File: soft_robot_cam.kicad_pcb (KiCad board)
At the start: 4 copper layers, 49.8 x 47.3 mm, 95 parts, among them J1 Connector, J10 Screw_Terminal_01x02, J11 Conn_02x02_Counter_Clockwise, J2 Conn_01x06, J3 Conn_01x03, J4 Conn_01x05_Pin, J5 Conn_01x02_Pin, J6 Screw_Terminal_01x02, J7 Screw_Terminal_01x02, J8 Conn_01x24_Socket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

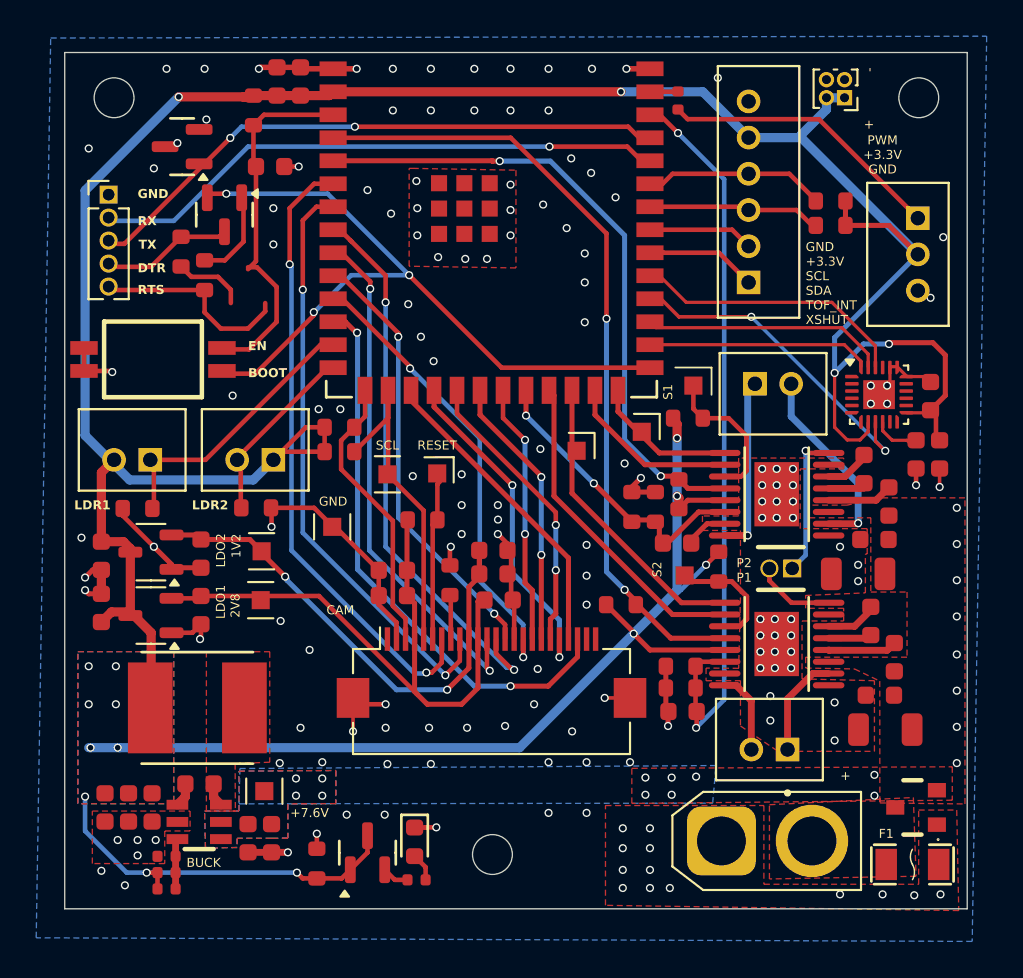
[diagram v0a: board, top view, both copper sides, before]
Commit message: Minor additions to PCB Layout, added branding and text
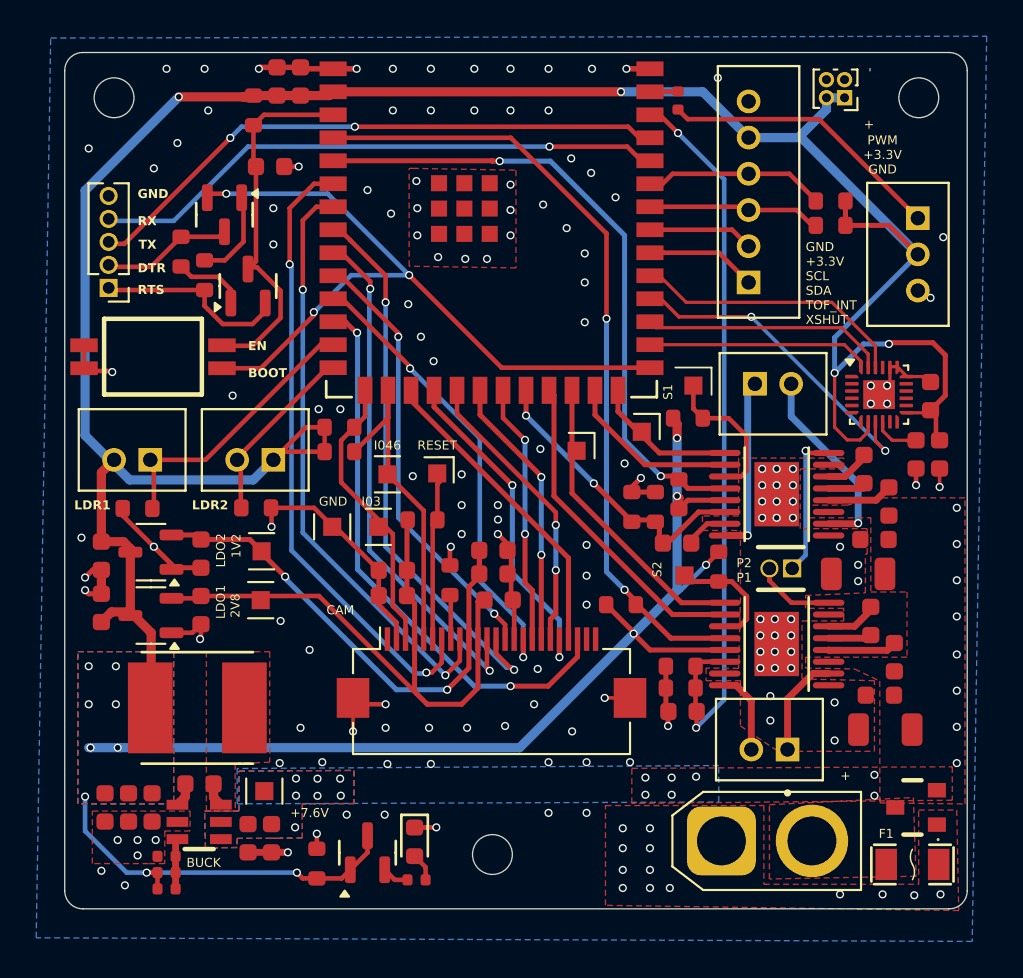
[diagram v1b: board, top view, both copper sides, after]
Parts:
- added G***: LOGO, LOGO, B.Cu at (164.4, 130.0)
- added GND: TestPoint_Pad_1.0x1.0mm, TestPoint:TestPoint_Pad_1.0x1.0mm, F.Cu at (175.6, 141.4)
- moved Q1 8.52 mm to (168.4, 128.1), turned to 90 degrees
- moved J4 5.15 mm to (160.7, 128.2), turned to 180 degrees
- moved SW4 0.15 mm to (163.2, 132.0)
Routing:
- net +7.6V: vias 11 -> 14
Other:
- outline, holes or cut-outs redrawn
- board text added: "Designed by: Evan Bhogal https://github.com/esb8/Soft-Robotics"
- board text added: "I03"
- board text added: "I046"
- board text added: "PROPERTY OF ELIXIR LABS"
- board text removed: "SCL"

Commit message: Minor Changes
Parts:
- removed the GND at (173.1, 141.4)
- removed the GND at (175.6, 141.4)
- removed the GND at (176.1, 138.5)
- added R25: 10kΩ, PCM_JLCPCB:R_0603, F.Cu at (191.8, 135.6)
- added REF**: TestPoint_Pad_1.0x1.0mm, TestPoint:TestPoint_Pad_1.0x1.0mm, F.Cu at (173.1, 141.4)
- added REF**: TestPoint_Pad_1.0x1.0mm, TestPoint:TestPoint_Pad_1.0x1.0mm, F.Cu at (176.1, 138.4)
- added REF**: TestPoint_Pad_1.0x1.0mm, TestPoint:TestPoint_Pad_1.0x1.0mm, F.Cu at (175.6, 141.4)
- moved G*** 3.13 mm to (165.4, 132.9)
- moved REF** 0.66 mm to (192.9, 132.9)
- moved R16 0.52 mm to (193.2, 135.6), turned to 90 degrees
- moved GND 0.35 mm to (186.5, 137.6)
- moved R9 0.15 mm to (162.2, 140.4)
- moved GND 0.11 mm to (190.1, 136.2)
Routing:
- net /IN1_A: track 8.02 -> 9.79 mm
- net GND: track 65.5 -> 66.5 mm
- net +3.3V: track 222.8 -> 223.4 mm
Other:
- board text added: "IN1B"
- board text added: "IO3"
- board text added: "IO45"
- board text added: "IO46"
- board text added: "PWM"
- board text added: "REDESIGN"
- board text added: "SCL"
- board text added: "SDA"
- board text added: "TOF_INT"
- board text added: "XSHUT"
- board text removed: "I03"
- board text removed: "I046"

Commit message: Cleaned Up BOM
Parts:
- F1: value JFC1206-1450FS -> BHFUSE BSMD1206C-1700T
- J8: footprint Connector_FFC-FPC:Hirose_FH12-24S-0.5SH_1x24-1MP_P0.50mm_Horizontal -> easyeda2kicad:FPC-SMD_AFC07-S24ECA-00
- L1: footprint easyeda2kicad:IND-SMD_L6.0-W6.0_SWPA6045S -> easyeda2kicad:IND-SMD_L6.0-W6.0
- moved J8 0.78 mm to (181.9, 148.7)
- moved F1 0.35 mm to (205.1, 159.7)
- moved L1 0.32 mm to (165.3, 151.5)
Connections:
- U9 pad 42: GND -> (no net)
- U9 pad 43: GND -> (no net)
- U9 pad 44: GND -> (no net)
- U9 pad 45: GND -> (no net)
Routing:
- net GND: track 66.5 -> 71.1 mm, vias 164 -> 160
- net +2V8: track 34.6 -> 35.4 mm, vias 0 -> 2
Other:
- board text removed: "REDESIGN"

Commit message: Critical Fixes
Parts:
- removed the REF** at (176.1, 138.4)
- added G***: LOGO, LOGO, B.Cu at (181.2, 121.2)
- moved R25 2.65 mm to (189.2, 135.6), turned to 0 degrees
- moved R3 1.70 mm to (173.4, 137.6)
- moved GND 1.52 mm to (191.5, 135.8)
- moved R24 1.45 mm to (173.4, 135.8)
- moved REF** 0.75 mm to (178.8, 139.2)
- moved C25 0.36 mm to (182.2, 145.1)
- moved F1 0.33 mm to (205.1, 160.0)
- moved C26 0.24 mm to (181.9, 142.5)
- moved C31 0.20 mm to (182.0, 143.8)
- moved REF** 0.10 mm to (193.0, 132.9)
- moved R23 0.05 mm to (200.6, 124.8)
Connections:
- R24 pad 2: /I2C_SCL -> /I2C_SDA
- R25 pad 1: /IN1_A -> GND
- R25 pad 2: GND -> Net-(U9-IO45)
- R3 pad 2: /I2C_SDA -> /I2C_SCL
- U9 pad 14: /LDR2 -> /I2C_SDA
- U9 pad 15: /I2C_SDA -> /I2C_SCL
- U9 pad 16: /I2C_SCL -> /LDR2
- U9 pad 26: /IN1_A -> Net-(U9-IO45)
- U9 pad 28: /MOSI1 -> /IN1_A
- U9 pad 29: /SCLK1 -> /MOSI1
- U9 pad 30: /MISO1 -> /SCLK1
- U9 pad 31: /CS1 -> /MISO1
- U9 pad 32: /XSHUT -> /CS1
- U9 pad 33: /TOF_INT -> /XSHUT
- U9 pad 42: (no net) -> GND
- U9 pad 43: (no net) -> GND
- U9 pad 44: (no net) -> GND
- U9 pad 45: (no net) -> GND
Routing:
- net /LDR2: track 10.2 -> 18.5 mm, vias 0 -> 2
- net /TOF_INT: track 5.98 -> 0.00 mm
- net +3.3V: track 223.4 -> 220.5 mm
- net /I2C_SCL: track 18.7 -> 16.3 mm
- net Net-(U9-IO45): track 0.00 -> 2.23 mm
- net /I2C_SDA: track 15.8 -> 17.5 mm
- net GND: track 71.1 -> 72.3 mm, vias 160 -> 161
- net /MOSI1: track 12.3 -> 13.3 mm
- net /CS1: track 15.2 -> 15.8 mm
- net /MISO1: track 18.3 -> 18.8 mm
- net /SCLK1: track 13.5 -> 14.0 mm
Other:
- board text removed: "IO45"
- board text removed: "IO46"
- board text removed: "PROPERTY OF ELIXIR LABS"

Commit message: Fixes the layout
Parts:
- removed J2: Conn_01x06, easyeda2kicad:JST_B6B-PH-K-S
- added J12: B5B-PH-K-S-(LF)(SN), easyeda2kicad:CONN-TH_B5B-PH-K-S-LF-SN, F.Cu at (196.0, 121.8)
- added R26: 10kΩ, PCM_JLCPCB:R_0603, F.Cu at (176.3, 136.5)
- moved C13 3.86 mm to (166.6, 119.1), turned to 180 degrees
- moved REF** 2.50 mm to (176.3, 139.0)
- moved R18 0.96 mm to (192.2, 116.9), turned to 90 degrees
- moved R25 0.07 mm to (189.1, 135.6)
- turned GND to -90 degrees
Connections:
- REF** pad : /I2C_SDA -> /I2C_SCL
- U9 pad 16: /LDR2 -> Net-(U9-IO46)
- U9 pad 33: /XSHUT -> /nFAULT_A
- U9 pad 5: /nFAULT_A -> /LDR2
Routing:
- net /nFAULT_A: track 35.7 -> 19.3 mm
- net /XSHUT: track 6.81 -> 0.00 mm
- net /LDR2: track 18.5 -> 25.3 mm, vias 2 -> 1
- net +3.3V: track 220.5 -> 226.4 mm
- net Net-(U9-IO46): track 0.00 -> 2.01 mm
- net /EN: track 20.0 -> 21.4 mm
- net GND: track 72.3 -> 73.5 mm, vias 161 -> 160
- net /S_PWM: track 15.7 -> 16.4 mm
- net /BOOT: track 40.5 -> 41.2 mm
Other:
- board text removed: "TOF_INT"
- board text removed: "XSHUT"

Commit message: Production ready PCB
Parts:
- removed J11: Conn_02x02_Counter_Clockwise, Connector_PinHeader_1.00mm:PinHeader_2x02_P1.00mm_Vertical
- added REF**: TestPoint_Pad_1.0x1.0mm, TestPoint:TestPoint_Pad_1.0x1.0mm, F.Cu at (178.2, 137.0)
- added U1: PZ127-2-02-Z, easyeda2kicad:HDR-TH_4P-P1.27-V-M-R2-C2-S1.27_MH127V-12-04-0820, F.Cu at (200.9, 117.4)
- moved REF** 0.22 mm to (176.4, 139.2)
- moved G*** 0.07 mm to (165.4, 133.0)
- turned REF** to -90 degrees
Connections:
- J12 pad 1: +3.3V -> /XSHUT
- U3 pad 22: /CS1 -> +3.3V
- U3 pad 23: /SCLK1 -> /SCL
- U3 pad 24: /MOSI1 -> /SDA
- U3 pad 9: /MISO1 -> unconnected-(U3-SDO/AD0-Pad9)
- U9 pad 28: /IN1_A -> unconnected-(U9-IO35-Pad28)
- U9 pad 29: /MOSI1 -> unconnected-(U9-IO36-Pad29)
- U9 pad 30: /SCLK1 -> unconnected-(U9-IO37-Pad30)
- U9 pad 31: /MISO1 -> /IN1_A
- U9 pad 32: /CS1 -> /nFAULT_A
- U9 pad 33: /nFAULT_A -> /XSHUT
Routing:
- net /MISO1: track 18.8 -> 0.00 mm, vias 2 -> 0
- net /CS1: track 15.8 -> 0.00 mm
- net /SCLK1: track 14.0 -> 0.00 mm
- net /MOSI1: track 13.3 -> 0.00 mm
- net /SCL: track 10.2 -> 20.6 mm
- net /SDA: track 9.59 -> 18.4 mm
- net /XSHUT: track 0.00 -> 6.34 mm
- net +3.3V: track 226.4 -> 222.0 mm
- net /IN1_A: track 9.99 -> 13.7 mm
- net Net-(U9-IO46): track 2.01 -> 4.16 mm
- net /nFAULT_A: track 19.3 -> 17.8 mm
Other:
- board text added: "GND +3.3V SCL SDA +3.3V"
- board text added: "IO46"
- board text removed: "GND +3.3V SCL SDA TOF_INT XSHUT"

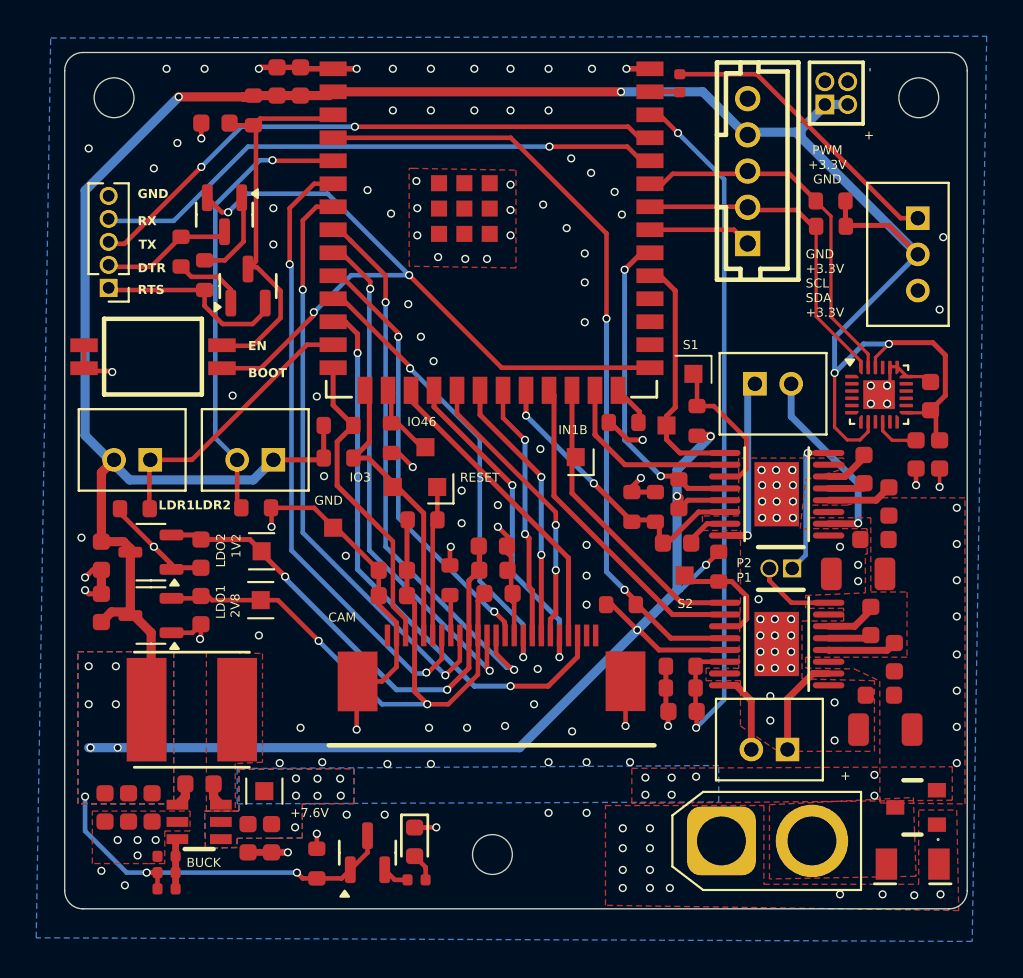
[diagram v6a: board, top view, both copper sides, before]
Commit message: Fixed Fuse, Added more testpads, changed xt30 to male, added switch in schematic for GPIO3
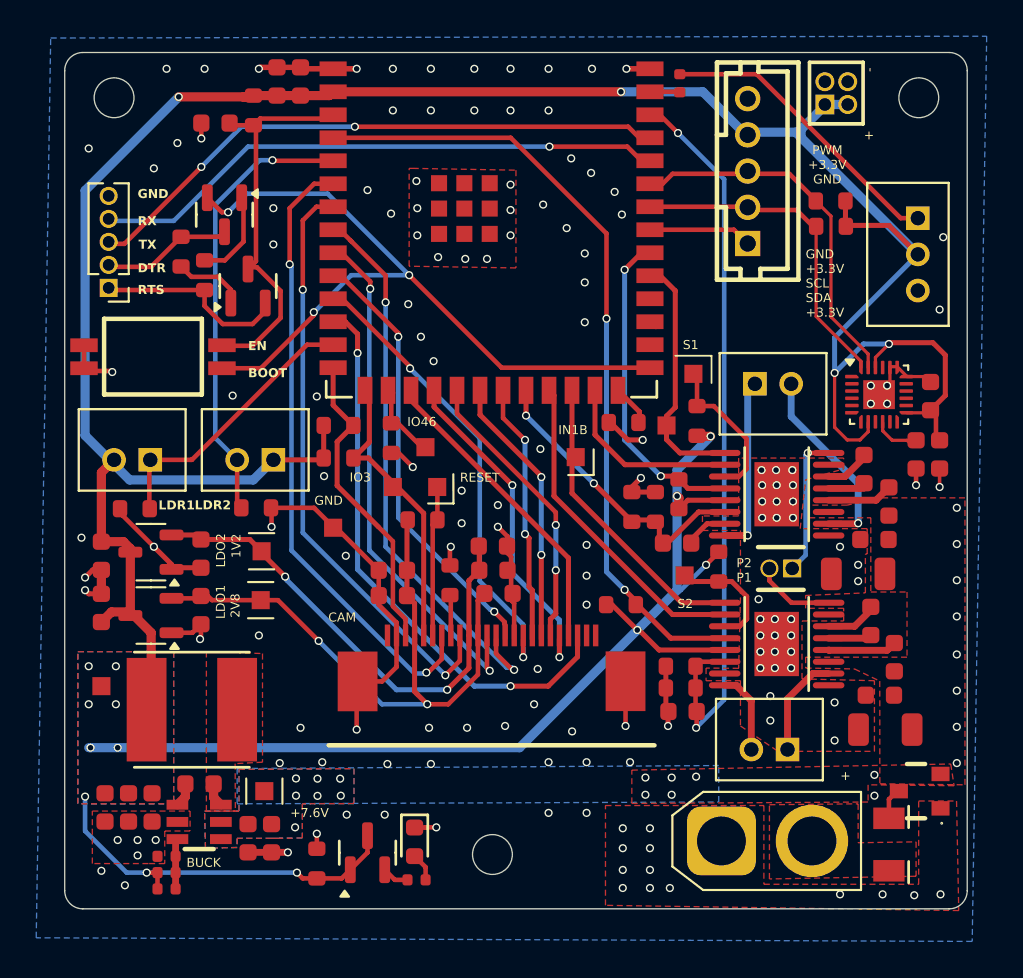
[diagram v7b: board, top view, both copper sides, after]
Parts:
- added REF**: TestPoint_Pad_1.0x1.0mm, TestPoint:TestPoint_Pad_1.0x1.0mm, F.Cu at (160.3, 150.2)
- moved F1 1.70 mm to (203.8, 158.9), turned to 90 degrees
- moved Q3 0.92 mm to (205.5, 156.0)
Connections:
- F1 pad 2: GND -> Net-(Q3-D)
- Q3 pad 3: Net-(J1-Pin_2) -> Net-(Q3-D)
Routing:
- net Net-(Q3-D): track 0.00 -> 1.66 mm
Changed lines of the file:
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@@
 	(net 87 "unconnected-(U9-IO37-Pad30)")
 	(net 88 "/XSHUT")
+	(net 89 "Net-(Q3-D)")
 	(footprint "PCM_JLCPCB:C_0603"
 		(layer "F.Cu")
@@
 		)
 	)
+	(footprint "TestPoint:TestPoint_Pad_1.0x1.0mm"
+		(layer "F.Cu")
+		(at 160.3 150.2)
+		(descr "SMD rectangular pad as test Point, square 1.0mm side length")
+		(tags "test point SMD pad rectangle square")
+		(property "Reference" "REF**"
+			(at 0 -1.448 0)
+			(layer "F.SilkS")
+			(hide yes)
+			(effects
+				(font
+					(size 1 1)
+					(thickness 0.153)
+				)
+			)
+		)
+		(property "Value" "TestPoint_Pad_1.0x1.0mm"
+			(at 0 1.55 0)
+			(layer "F.Fab")
+			(effects
+				(font
+					(size 1 1)
+					(thickness 0.153)
+				)
+			)
+		)
+		(property "Datasheet" ""
+			(at 0 0 0)
+			(unlocked yes)
+			(layer "F.Fab")
+			(hide yes)
+			(effects
+				(font
+					(size 1.27 1.27)
+					(thickness 0.153)
+				)
+			)
+		)
+		(property "Description" ""
+			(at 0 0 0)
+			(unlocked yes)
+			(layer "F.Fab")
+			(hide yes)
+			(effects
+				(font
+					(size 1.27 1.27)
+					(thickness 0.153)
+				)
+			)
+		)
+		(attr exclude_from_pos_files exclude_from_bom)
+		(fp_line
+			(start -1 -1)
+			(end -1 1)
+			(stroke
+				(width 0.05)
+				(type solid)
+			)
+			(layer "F.CrtYd")
+		)
+		(fp_line
+			(start -1 -1)
+			(end 1 -1)
+			(stroke
+				(width 0.05)
+				(type solid)
+			)
+			(layer "F.CrtYd")
+		)
+		(fp_line
+			(start 1 1)
+			(end -1 1)
+			(stroke
+				(width 0.05)
+				(type solid)
+			)
+			(layer "F.CrtYd")
+		)
+		(fp_line
+			(start 1 1)
+			(end 1 -1)
+			(stroke
+				(width 0.05)
+				(type solid)
+			)
+			(layer "F.CrtYd")
+		)
+		(pad "" smd rect
+			(at 0 0)
+			(size 1 1)
+			(layers "F.Cu" "F.Mask")
+			(net 7 "+3.3V")
+		)
+		(embedded_fonts no)
+	)
 	(footprint "PCM_JLCPCB:R_0603"
 		(layer "F.Cu")
@@
 	(footprint "easyeda2kicad:SOT-23_L2.9-W1.3-P1.90-LS2.4-BR"
 		(layer "F.Cu")
-		(at 205.3 156.9)
+		(at 205.5 156)
 		(property "Reference" "Q3"
 			(at 0 -4.95 0)
@@
 			(size 1 0.8)
 			(layers "F.Cu" "F.Mask" "F.Paste")
-			(net 23 "Net-(J1-Pin_2)")
+			(net 89 "Net-(Q3-D)")
 			(pinfunction "D")
 			(pintype "unspecified")
@@
 	(footprint "easyeda2kicad:F1206"
 		(layer "F.Cu")
-		(at 205.113409 160.028352)
+		(at 203.8 158.95 90)
 		(property "Reference" "F1"
-			(at 0 -4 0)
+			(at 0 -4 90)
 			(layer "F.SilkS")
 			(hide yes)
@@
 		)
 		(property "Value" "BHFUSE BSMD1206C-1700T"
-			(at 0 4 0)
+			(at 0 4 90)
 			(layer "F.Fab")
 			(effects
@@
 		)
 		(property "Datasheet" "https://lcsc.com/product-detail/Surface-Mount-Fuses_4-5A-32V_C136350.html"
-			(at 0 0 0)
+			(at 0 0 90)
 			(layer "F.Fab")
 			(hide yes)
@@
 		)
 		(property "Description" "150A Surface Mount Fuse 7A 32V 1206 Disposable fuses ROHS"
-			(at 0 0 0)
+			(at 0 0 90)
 			(layer "F.Fab")
 			(hide yes)
@@
 		)
 		(property "LCSC Part" "C41367230"
-			(at 0 0 0)
+			(at 0 0 90)
 			(unlocked yes)
 			(layer "F.Fab")
@@
 		)
 		(property "LCSC" "C41367230"
-			(at 0 0 0)
+			(at 0 0 90)
 			(unlocked yes)
 			(layer "F.Fab")
@@
 		(attr smd)
 		(fp_line
-			(start -2.12 1.09)
-			(end -0.93 1.09)
+			(start 2.12 1.09)
+			(end 0.93 1.09)
 			(stroke
 				(width 0.15)
@@
 		)
 		(fp_line
-			(start 2.12 1.09)
-			(end 0.93 1.09)
+			(start -2.12 1.09)
+			(end -0.93 1.09)
 			(stroke
 				(width 0.15)
@@
 		)
 		(fp_text user "${REFERENCE}"
-			(at 0 0 0)
+			(at 0 0 90)
 			(layer "F.Fab")
 			(effects
@@
 		)
 		(pad "1" smd rect
-			(at -1.45 0)
+			(at -1.45 0 90)
 			(size 1.19 1.73)
 			(layers "F.Cu" "F.Mask" "F.Paste")
@@
 		)
 		(pad "2" smd rect
-			(at 1.45 0)
+			(at 1.45 0 90)
 			(size 1.19 1.73)
 			(layers "F.Cu" "F.Mask" "F.Paste")
-			(net 6 "GND")
+			(net 89 "Net-(Q3-D)")
 			(pinfunction "2")
 			(pintype "unspecified")
@@
 	)
 	(segment
+		(start 172.05 140.35)
+		(end 173 141.3)
+		(width 0.254)
+		(layer "F.Cu")
+		(net 6)
+	)
+	(segment
 		(start 169.699963 159.38)
 		(end 168.4 159.38)
@@
 	)
 	(segment
-		(start 172.05 140.35)
-		(end 173 141.3)
-		(width 0.254)
-		(layer "F.Cu")
-		(net 6)
-	)
-	(segment
 		(start 173.1 116.1)
 		(end 174.2 116.1)
@@
 	)
 	(segment
+		(start 169.67 140.35)
+		(end 172.05 140.35)
+		(width 0.254)
+		(layer "F.Cu")
+		(net 6)
+	)
+	(segment
 		(start 191.48 151.58)
 		(end 191.48 149.1)
@@
 	)
 	(segment
-		(start 169.67 140.35)
-		(end 172.05 140.35)
-		(width 0.254)
-		(layer "F.Cu")
-		(net 6)
-	)
-	(segment
 		(start 189.6 139.2)
 		(end 190.1 138.7)
@@
 		(net 88)
 	)
+	(segment
+		(start 203.8 157.4)
+		(end 203.8 156.45)
+		(width 0.254)
+		(layer "F.Cu")
+		(net 89)
+	)
+	(segment
+		(start 203.8 156.45)
+		(end 204.3 155.95)
+		(width 0.254)
+		(layer "F.Cu")
+		(net 89)
+	)
 	(zone
 		(net 11)
@@
 		(polygon
 			(pts
-				(xy 199.2 148.6) (xy 199.2 149.2) (xy 201.9 149.25) (xy 203.294803 149.919335) (xy 203.3 156.65)
-				(xy 208 156.707317) (xy 208 139.8) (xy 203.3 139.8) (xy 201.5 140.2) (xy 199.4 140.2) (xy 199.4 140.9)
+				(xy 199.2 148.6) (xy 199.2 149.2) (xy 201.9 149.25) (xy 203.294803 149.919335) (xy 203.299184 155.592704)
+				(xy 208 155.650031) (xy 208 139.8) (xy 203.3 139.8) (xy 201.5 140.2) (xy 199.4 140.2) (xy 199.4 140.9)
 				(xy 202.8 140.9) (xy 202.8 145) (xy 204.8 145) (xy 204.8 148.6) (xy 199.5 148.6)
 			)
@@
 		(polygon
 			(pts
-				(xy 196.893868 161.143381) (xy 205.443868 161.143381) (xy 205.443868 157.043381) (xy 207.545868 157.043381)
+				(xy 196.893868 161.143381) (xy 205.443868 161.143381) (xy 205.443868 156.543381) (xy 207.535868 156.543381)
 				(xy 207.656898 162.594939) (xy 188.143868 162.307082) (xy 188.143868 156.793381) (xy 196.893868 156.793381)
 			)
@@
 		(polygon
 			(pts
-				(xy 205.15 156.35) (xy 205.3 160.7) (xy 197.2 160.849904) (xy 197.2 156.75)
+				(xy 202.1 156.7) (xy 202.1 158.85) (xy 205.3 158.8) (xy 205.3 160.7) (xy 197.2 160.849904) (xy 197.2 156.75)
 			)
 		)
@@
 		(polygon
 			(pts
-				(xy 207.3 154.654128) (xy 207.3 156.5) (xy 189.6 156.677889) (xy 189.6 154.739401)
+				(xy 207.215339 154.499704) (xy 207.4 155.7) (xy 202.65 155.65) (xy 202.65 156.6) (xy 189.6 156.677889)
+				(xy 189.6 154.839401)
 			)
 		)
